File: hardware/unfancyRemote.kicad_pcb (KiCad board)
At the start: 2 copper layers, 30.5 x 61 mm, 35 parts, among them J1 Arduino Analog, J2 Arduino Digital, J3 HALL1, J4 HALL2, J5 PPM, J6 Conn_01x02, Q1 AO3401A, Q2 MMBT3904, SW1 SW_Push, U1 E28-2G4M12S

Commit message: Updates to PCB v1.0, simple disconnect detection on the remote
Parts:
- moved R7 1.71 mm to (121.9, 71.9)
- moved D3 1.63 mm to (121.9, 73.9)
- moved R8 1.55 mm to (121.9, 78.5)
- moved D4 1.48 mm to (121.9, 80.5)
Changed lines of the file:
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@@
   )
   (footprint "LED_SMD:LED_0805_2012Metric" (layer "F.Cu")
-    (at 120.65 74.93 180)
+    (at 121.92 73.914 180)
     (descr "LED SMD 0805 (2012 Metric), square (rectangular) end terminal, IPC_7351 nominal, (Body size source: https://docs.google.com/spreadsheets/d/1BsfQQcO9C6DZCsRaXUlFlo91Tg2WpOkGARC1WS5S8t0/edit?usp=sharing), generated with kicad-footprint-generator")
     (tags "LED")
@@
   )
   (footprint "LED_SMD:LED_0805_2012Metric" (layer "F.Cu")
-    (at 120.65 81.28 180)
+    (at 121.92 80.518 180)
     (descr "LED SMD 0805 (2012 Metric), square (rectangular) end terminal, IPC_7351 nominal, (Body size source: https://docs.google.com/spreadsheets/d/1BsfQQcO9C6DZCsRaXUlFlo91Tg2WpOkGARC1WS5S8t0/edit?usp=sharing), generated with kicad-footprint-generator")
     (tags "LED")
@@
   )
   (footprint "Resistor_SMD:R_0603_1608Metric" (layer "F.Cu")
-    (at 120.65 73.025)
+    (at 121.92 71.882)
     (descr "Resistor SMD 0603 (1608 Metric), square (rectangular) end terminal, IPC_7351 nominal, (Body size source: IPC-SM-782 page 72, https://www.pcb-3d.com/wordpress/wp-content/uploads/ipc-sm-782a_amendment_1_and_2.pdf), generated with kicad-footprint-generator")
     (tags "resistor")
@@
   )
   (footprint "Resistor_SMD:R_0603_1608Metric" (layer "F.Cu")
-    (at 120.65 79.375)
+    (at 121.92 78.486)
     (descr "Resistor SMD 0603 (1608 Metric), square (rectangular) end terminal, IPC_7351 nominal, (Body size source: IPC-SM-782 page 72, https://www.pcb-3d.com/wordpress/wp-content/uploads/ipc-sm-782a_amendment_1_and_2.pdf), generated with kicad-footprint-generator")
     (tags "resistor")
@@
   (segment (start 138.3405 93.345) (end 138.43 93.4345) (width 0.25) (layer "B.Cu") (net 32))
   (segment (start 138.43 93.4345) (end 138.43 105.41) (width 0.25) (layer "B.Cu") (net 32))
-  (segment (start 119.7125 75.2325) (end 120.015 74.93) (width 0.25) (layer "F.Cu") (net 33))
   (zone (net 2) (net_name "GND") (layers F&B.Cu) (hatch edge 0.508)
     (connect_pads (clearance 0.508))

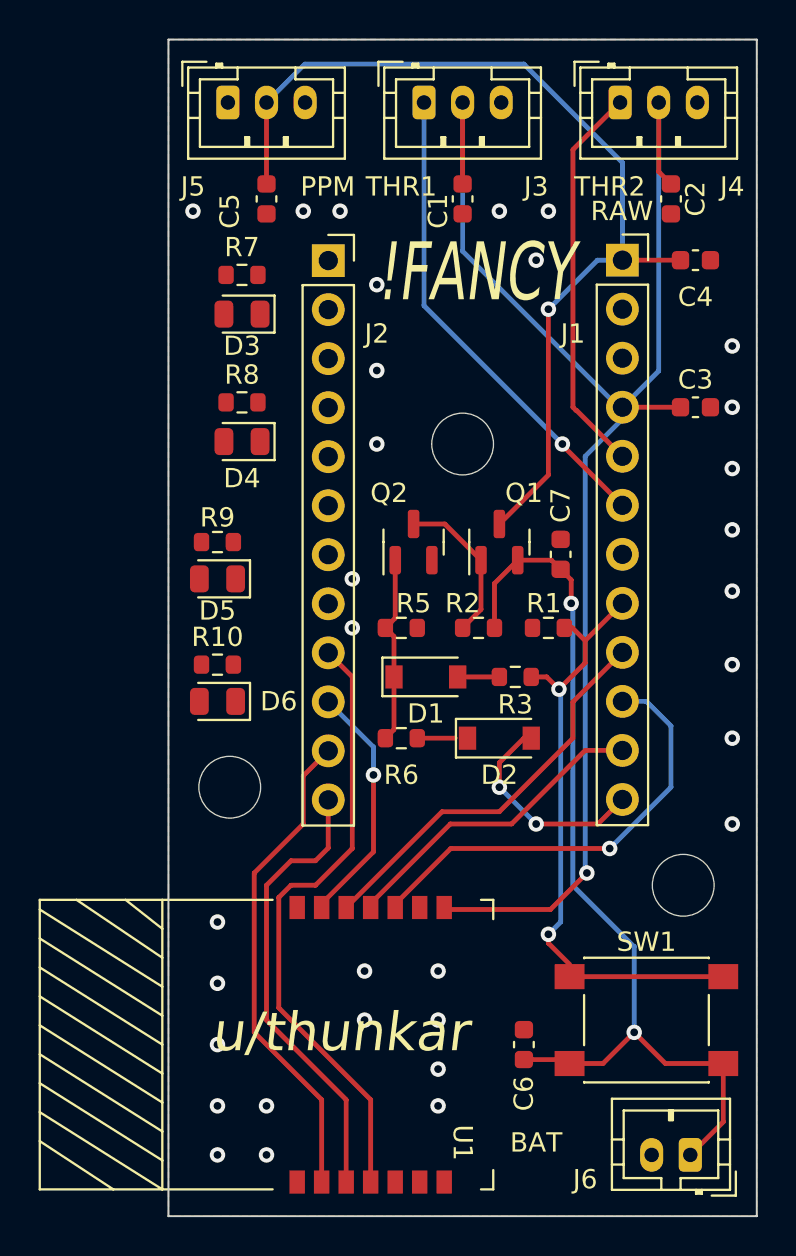
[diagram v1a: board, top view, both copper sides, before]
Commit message: Added library, PCB 1.0, software scheduler
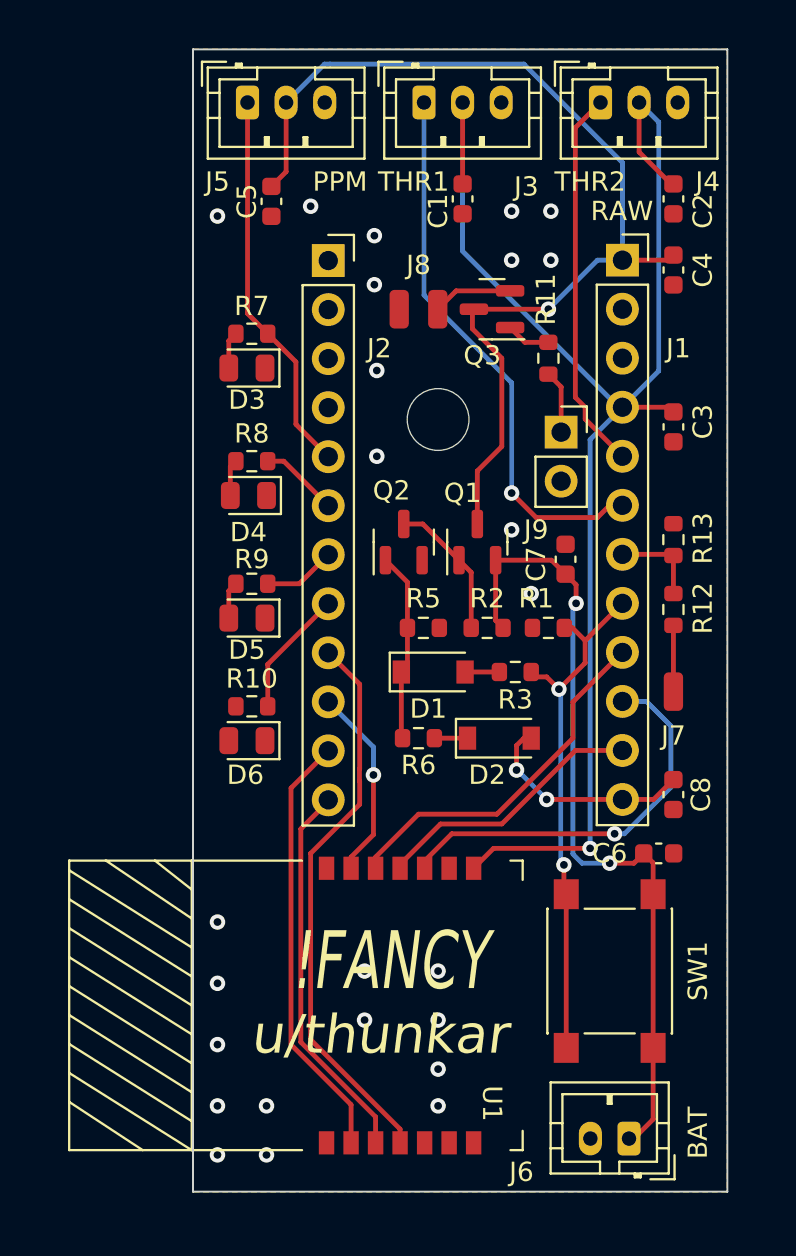
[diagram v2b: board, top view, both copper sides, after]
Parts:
- removed the   at (144.8, 103.5)
- removed the   at (121.3, 98.4)
- added C8: 1uF, Capacitor_SMD:C_0603_1608Metric, F.Cu at (144.3, 98.8)
- added J7: VBAT, Connector_wire:SolderWirePad_1x01_SMD_1x2mm, F.Cu at (144.3, 93.5)
- added J8: Motor, unfancyRemote_components:SolderWirePad_1x02_SMD_1x2mm, F.Cu at (131.1, 73.7)
- added J9: Extra analog 1, Connector_PinSocket_2.54mm:PinSocket_1x02_P2.54mm_Vertical, F.Cu at (138.5, 80.0)
- added Q3: MMBT3904, Package_TO_SOT_SMD:SOT-23, F.Cu at (134.9, 73.7)
- added R11: 1K, Resistor_SMD:R_0603_1608Metric, F.Cu at (137.8, 76.2)
- added R12: 100K, Resistor_SMD:R_0603_1608Metric, F.Cu at (144.3, 89.2)
- added R13: 6.8K, Resistor_SMD:R_0603_1608Metric, F.Cu at (144.3, 85.6)
- J6: value Conn_01x02 -> VIN
- moved C6 12.1 mm to (143.5, 101.9), turned to 0 degrees
- moved J6 3.29 mm to (142.0, 116.6)
- moved SW1 3.17 mm to (141.0, 108.0), turned to 90 degrees
- moved R7 3.09 mm to (122.4, 74.9)
- moved R8 3.09 mm to (122.4, 81.5)
- moved D4 2.81 mm to (122.3, 83.3)
- moved D3 2.81 mm to (122.2, 76.7)
- moved R9 2.80 mm to (122.4, 87.9)
- moved R10 2.80 mm to (122.4, 94.2)
- moved D5 2.54 mm to (122.2, 89.7)
- moved U1 2.54 mm to (121.2, 109.2)
- moved D6 2.54 mm to (122.2, 96.0)
- moved   1.80 mm to (132.1, 79.4)
- moved C3 1.53 mm to (144.3, 79.8), turned to -90 degrees
- moved C4 1.25 mm to (144.3, 71.6), turned to -90 degrees
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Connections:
- C6 pad 1: VBAT -> 5VRAW
- C7 pad 1: VBAT -> 5VRAW
- J1 pad 7: VBAT -> VBATSCALED
- J6 pad 1: VBAT -> 5VRAW
- Q1 pad 2: VBAT -> 5VRAW
- R2 pad 1: VBAT -> 5VRAW
- SW1 pad 2: VBAT -> 5VRAW
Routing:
- net VBAT: track 49.2 -> 0.00 mm, vias 2 -> 0
- net 5VRAW: track 0.00 -> 42.6 mm, vias 0 -> 2
- net PPM: track 0.00 -> 20.1 mm
- net L4: track 0.00 -> 6.61 mm
- net VBATSCALED: track 0.00 -> 4.64 mm
- net Net-(Q3-Pad2): track 0.00 -> 4.14 mm
- net L2: track 0.00 -> 4.09 mm
- net BSENSE: track 31.8 -> 28.0 mm
- net L3: track 0.00 -> 3.76 mm
- net /RFBUSY: track 23.5 -> 20.0 mm
- net Net-(R12-Pad1): track 0.00 -> 3.43 mm
- net HALL1: track 25.3 -> 28.6 mm
- net +5V: track 50.6 -> 53.9 mm
- net MOTOR: track 0.00 -> 3.28 mm
- net /DIO1: track 32.1 -> 29.0 mm
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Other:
- board size 30.5 x 61 mm -> 27.7 x 59.2 mm
